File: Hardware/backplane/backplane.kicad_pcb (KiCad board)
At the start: 2 copper layers, 99.9 x 99.9 mm, 60 parts, among them J1 USB_B_Micro, SW1 SW_SPST, U1 74HC161, U2 MAX811SEUS-T, U3 MAX811SEUS-T, U4 PAL24, X1 24MHz

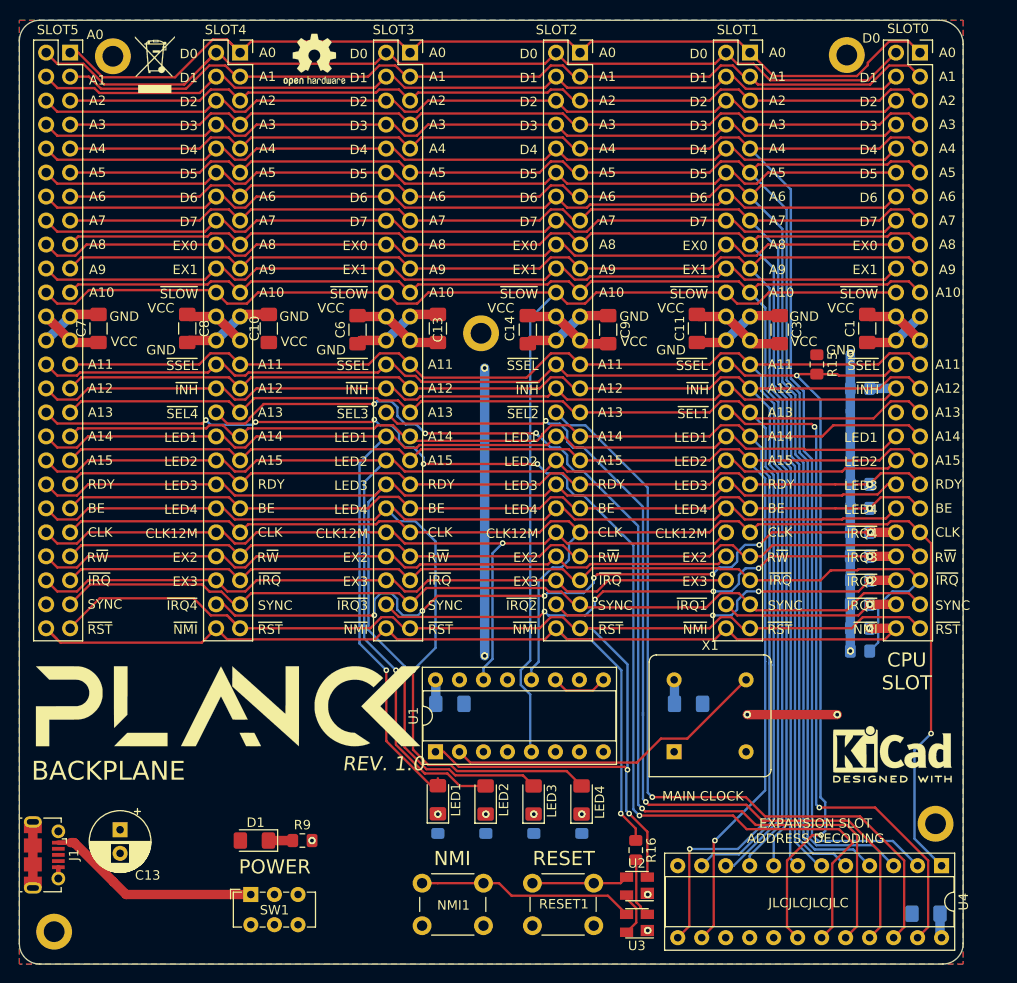
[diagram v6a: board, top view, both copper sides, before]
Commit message: each slot gets it's own slow signal
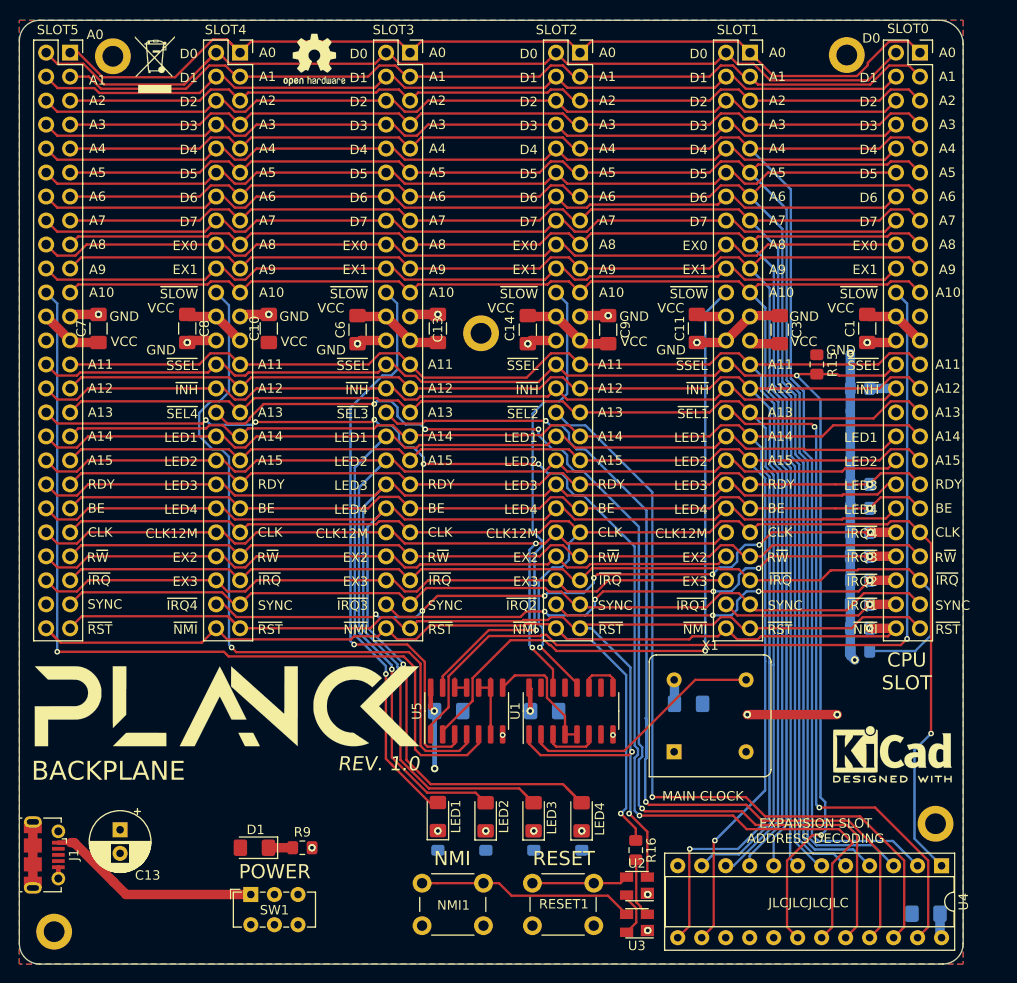
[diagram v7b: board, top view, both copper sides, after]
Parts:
- added C5: C_Small, Capacitor_SMD:C_1206_3216Metric_Pad1.42x1.75mm_HandSolder, B.Cu at (55.6, 73.2)
- added U5: 74AC11, Package_SO:SOIC-14_3.9x8.7mm_P1.27mm, F.Cu at (47.4, 73.2)
- U1: value 74HC161 -> 74AC161; footprint Package_DIP:DIP-16_W7.62mm_Socket -> Package_SO:SOIC-16_3.9x9.9mm_P1.27mm
- moved U1 15.0 mm to (58.4, 73.2)
- moved LED1 1.78 mm to (44.3, 84.3)
- moved LED2 1.78 mm to (49.4, 84.4)
- moved LED3 1.78 mm to (54.5, 84.4)
- moved LED4 1.78 mm to (59.5, 84.4)
- moved R10 1.78 mm to (44.3, 86.9)
- moved R11 1.78 mm to (49.4, 86.9)
- moved R12 1.78 mm to (54.5, 86.9)
- moved R13 1.78 mm to (59.6, 86.9)
- moved C2 0.77 mm to (45.5, 73.2)
- moved D1 0.76 mm to (24.9, 87.6)
- moved R9 0.76 mm to (30.0, 87.6)
- moved G*** 0.13 mm to (22.0, 72.6)
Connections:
- SLOT0 pad 22: ~SLOW~ -> ~SLOW0~
- SLOT1 pad 22: ~SLOW~ -> ~SLOW1~
- SLOT2 pad 22: ~SLOW~ -> ~SLOW2~
- SLOT3 pad 22: ~SLOW~ -> ~SLOW3~
- SLOT4 pad 22: ~SLOW~ -> ~SLOW4~
- SLOT5 pad 22: ~SLOW~ -> ~SLOW5~
- U1 pad 4: +5V -> Net-(U1-Pad4)
- U1 pad 5: ~SLOW~ -> Net-(U1-Pad4)
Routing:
- net ~SLOW~: track 145.7 -> 0.00 mm
- net ~SLOW0~: track 0.00 -> 95.2 mm, vias 0 -> 1
- net ~SLOW5~: track 0.00 -> 94.2 mm, vias 0 -> 1
- net ~SLOW4~: track 0.00 -> 78.2 mm, vias 0 -> 1
- net ~SLOW1~: track 0.00 -> 72.9 mm, vias 0 -> 1
- net ~SLOW3~: track 0.00 -> 61.9 mm, vias 0 -> 1
- net ~SLOW2~: track 0.00 -> 52.6 mm, vias 0 -> 1
- net +5V: track 124.6 -> 106.4 mm, vias 4 -> 5
- net GND: track 70.1 -> 52.2 mm, vias 5 -> 17
- net Net-(U1-Pad4): track 0.00 -> 13.4 mm
- net ~RESET~: track 148.8 -> 138.8 mm
- net /CLK_24M: track 34.5 -> 26.1 mm
- net Net-(U5-Pad10): track 0.00 -> 8.17 mm
- net SLOT3: track 101.4 -> 105.3 mm
- net LED3: track 140.4 -> 144.3 mm
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
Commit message: Many updates. SLOW signal is now shared amongst all slots, so their output has to be open drain.
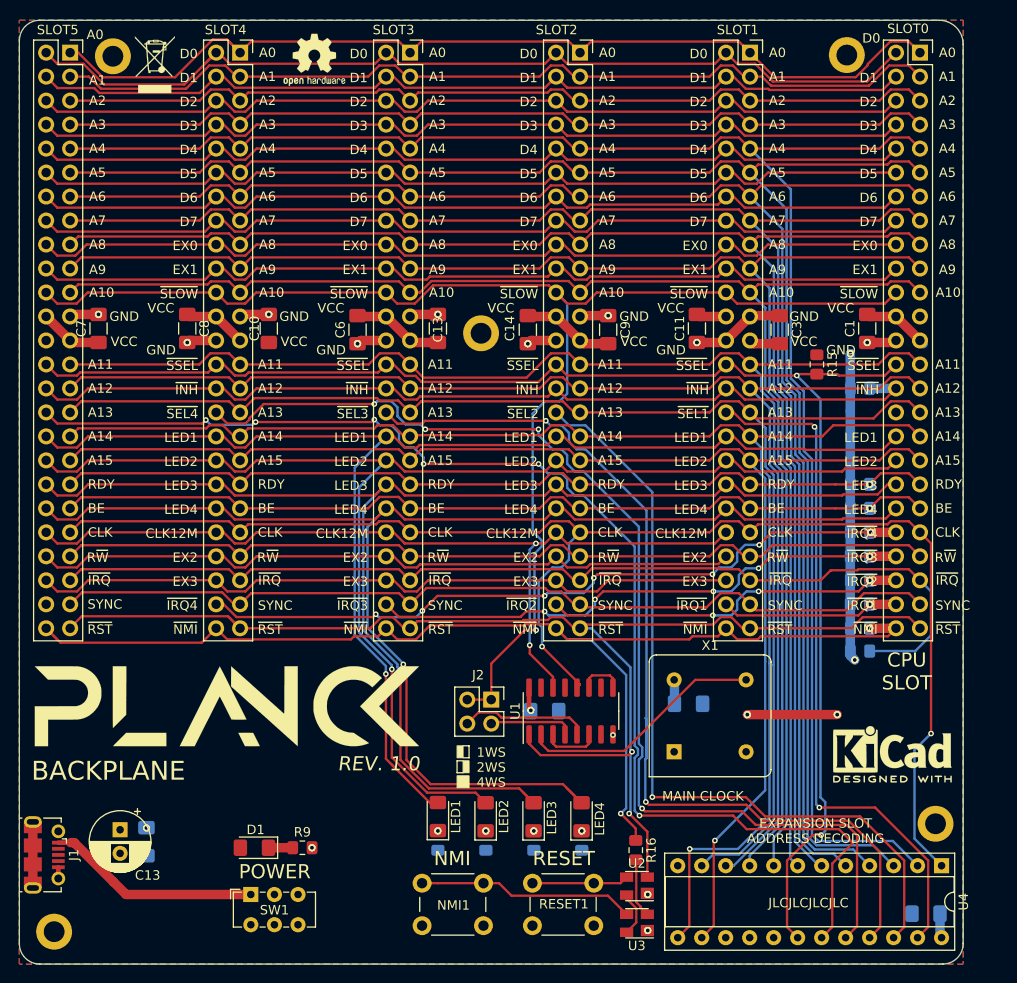
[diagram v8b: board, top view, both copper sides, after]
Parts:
- removed U5: 74AC11, Package_SO:SOIC-14_3.9x8.7mm_P1.27mm
- added J2: Conn_02x02_Odd_Even, Connector_PinHeader_2.54mm:PinHeader_2x02_P2.54mm_Vertical, F.Cu at (50.0, 71.9)
- moved C2 34.9 mm to (13.5, 87.0), turned to 270 degrees
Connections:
- net SLOT1 renamed ~SLOT1~
- net SLOT2 renamed ~SLOT2~
- net SLOT3 renamed ~SLOT3~
- net SLOT4 renamed ~SLOT4~
- net SLOT5 renamed ~SLOT5~
- SLOT0 pad 22: ~SLOW0~ -> ~SLOW~
- SLOT1 pad 22: ~SLOW1~ -> ~SLOW~
- SLOT2 pad 22: ~SLOW2~ -> ~SLOW~
- SLOT3 pad 22: ~SLOW3~ -> ~SLOW~
- SLOT4 pad 22: ~SLOW4~ -> ~SLOW~
- SLOT5 pad 22: ~SLOW5~ -> ~SLOW~
- U1 pad 4: Net-(U1-Pad4) -> /DS1
- U1 pad 5: Net-(U1-Pad4) -> /DS2
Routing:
- net ~SLOW~: track 0.00 -> 147.9 mm, vias 0 -> 1
- net ~SLOW0~: track 95.2 -> 0.00 mm, vias 1 -> 0
- net ~SLOW5~: track 94.2 -> 0.00 mm, vias 1 -> 0
- net ~SLOW4~: track 78.2 -> 0.00 mm, vias 1 -> 0
- net ~SLOW1~: track 72.9 -> 0.00 mm, vias 1 -> 0
- net ~SLOW3~: track 61.9 -> 0.00 mm, vias 1 -> 0
- net ~SLOW2~: track 52.6 -> 0.00 mm, vias 1 -> 0
- net /DS2: track 0.00 -> 13.6 mm
- net Net-(U1-Pad4): track 13.4 -> 0.00 mm
- net /DS1: track 0.00 -> 8.99 mm
- net +5V: track 106.4 -> 97.6 mm, vias 5 -> 4
- net Net-(U5-Pad10): track 8.17 -> 0.00 mm
- net Net-(U5-Pad11): track 2.25 -> 0.00 mm
- net GND: vias 17 -> 16
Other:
- board text added: "1WS"
- board text added: "2WS"
- board text added: "4WS"
